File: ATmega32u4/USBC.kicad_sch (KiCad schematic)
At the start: 6 parts, among them J1 USB_C_Receptacle_USB2.0, U4 USBLC6-2SC6

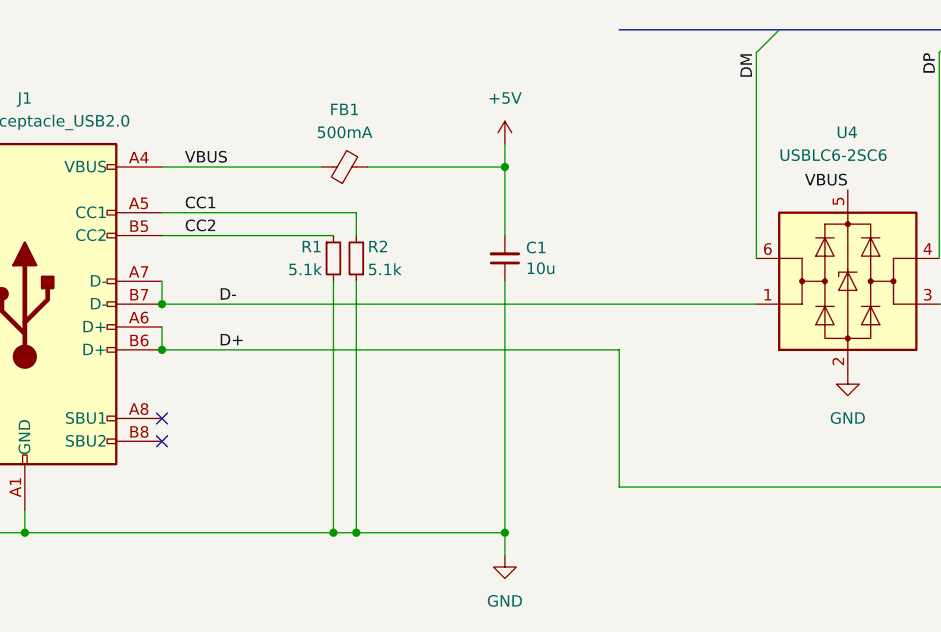
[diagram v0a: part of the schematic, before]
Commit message: Review and updates to power path
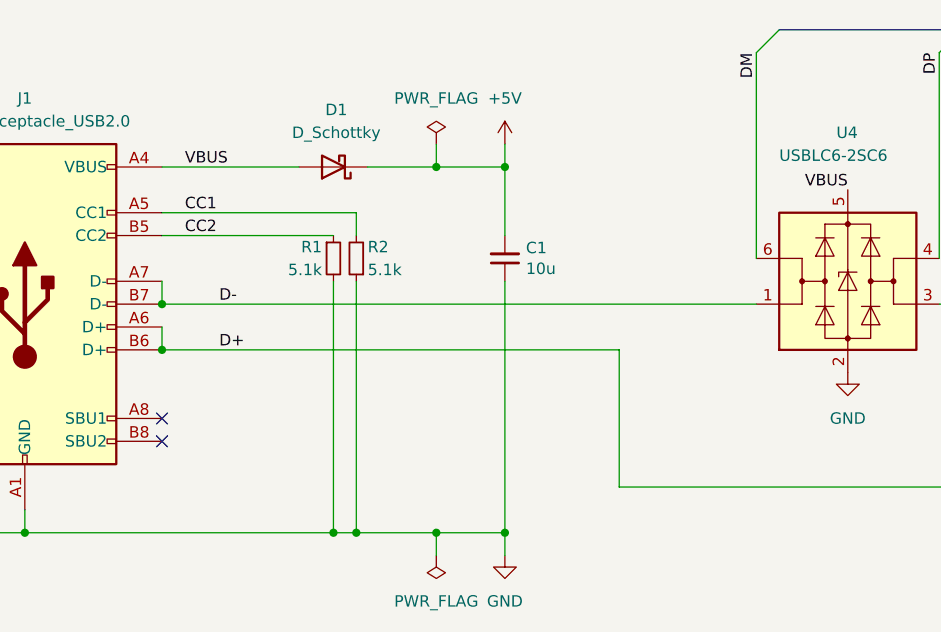
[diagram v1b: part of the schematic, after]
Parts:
- removed FB1: 500mA, Inductor_SMD:L_0805_2012Metric, symbol Device:FerriteBead_Small
- added D1: D_Schottky, Diode_SMD:D_SOD-323, symbol Device:D_Schottky
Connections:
- net +5V: now also D1.1 (K)
- net VBUS: now also D1.2 (A)
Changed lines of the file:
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@@
   (junction (at 165.1 106.68) (diameter 0) (color 0 0 0 0)
+  )
+  (junction (at 157.48 106.68) (diameter 0) (color 0 0 0 0)
+  )
+  (junction (at 157.48 66.04) (diameter 0) (color 0 0 0 0)
   )
   (junction (at 111.76 106.68) (diameter 0) (color 0 0 0 0)
@@
     (stroke (width 0) (type default) (color 0 0 0 0))
   )
-  (wire (pts (xy 148.59 106.68) (xy 165.1 106.68))
+  (wire (pts (xy 157.48 106.68) (xy 165.1 106.68))
     (stroke (width 0) (type default) (color 0 0 0 0))
   )
@@
     (stroke (width 0) (type default) (color 0 0 0 0))
   )
+  (wire (pts (xy 157.48 109.22) (xy 157.48 106.68))
+    (stroke (width 0) (type default) (color 0 0 0 0))
+  )
   (wire (pts (xy 104.14 106.68) (xy 111.76 106.68))
     (stroke (width 0) (type default) (color 0 0 0 0))
@@
     (stroke (width 0) (type default) (color 0 0 0 0))
   )
-  (bus (pts (xy 177.8 50.8) (xy 195.58 50.8))
-    (stroke (width 0) (type default) (color 0 0 0 0))
-  )
   (wire (pts (xy 148.59 78.74) (xy 148.59 106.68))
     (stroke (width 0) (type default) (color 0 0 0 0))
@@
     (stroke (width 0) (type default) (color 0 0 0 0))
   )
+  (wire (pts (xy 148.59 106.68) (xy 157.48 106.68))
+    (stroke (width 0) (type default) (color 0 0 0 0))
+  )
   (wire (pts (xy 165.1 109.22) (xy 165.1 106.68))
     (stroke (width 0) (type default) (color 0 0 0 0))
   )
-  (wire (pts (xy 127 66.04) (xy 144.78 66.04))
+  (wire (pts (xy 127 66.04) (xy 142.24 66.04))
+    (stroke (width 0) (type default) (color 0 0 0 0))
+  )
+  (wire (pts (xy 157.48 66.04) (xy 165.1 66.04))
     (stroke (width 0) (type default) (color 0 0 0 0))
   )
@@
     (stroke (width 0) (type default) (color 0 0 0 0))
   )
-  (wire (pts (xy 149.86 66.04) (xy 165.1 66.04))
+  (wire (pts (xy 157.48 63.5) (xy 157.48 66.04))
+    (stroke (width 0) (type default) (color 0 0 0 0))
+  )
+  (wire (pts (xy 149.86 66.04) (xy 157.48 66.04))
     (stroke (width 0) (type default) (color 0 0 0 0))
   )
@@
     )
     (property "Datasheet" "" (id 3) (at 203.2 88.9 0)
+      (effects (font (size 1.27 1.27)) hide)
+    )
+    (pin "1")
+  )
+  (symbol (lib_id "power:PWR_FLAG") (at 157.48 63.5 0) (unit 1)
+    (in_bom yes) (on_board yes) (fields_autoplaced)
+    (property "Reference" "#FLG01" (id 0) (at 157.48 61.595 0)
+      (effects (font (size 1.27 1.27)) hide)
+    )
+    (property "Value" "PWR_FLAG" (id 1) (at 157.48 58.42 0))
+    (property "Footprint" "" (id 2) (at 157.48 63.5 0)
+      (effects (font (size 1.27 1.27)) hide)
+    )
+    (property "Datasheet" "~" (id 3) (at 157.48 63.5 0)
       (effects (font (size 1.27 1.27)) hide)
     )
@@
     )
     (property "Datasheet" "~" (id 3) (at 148.59 76.2 0)
-      (effects (font (size 1.27 1.27)) hide)
-    )
-    (pin "1")
-    (pin "2")
-  )
-  (symbol (lib_id "Device:FerriteBead_Small") (at 147.32 66.04 90) (unit 1)
-    (in_bom yes) (on_board yes) (fields_autoplaced)
-    (property "Reference" "FB1" (id 0) (at 147.2819 59.69 90))
-    (property "Value" "500mA" (id 1) (at 147.2819 62.23 90))
-    (property "Footprint" "Inductor_SMD:L_0805_2012Metric" (id 2) (at 147.32 67.818 90)
-      (effects (font (size 1.27 1.27)) hide)
-    )
-    (property "Datasheet" "~" (id 3) (at 147.32 66.04 0)
       (effects (font (size 1.27 1.27)) hide)
     )
@@
     (pin "6")
   )
+  (symbol (lib_id "Device:D_Schottky") (at 146.05 66.04 180) (unit 1)
+    (in_bom yes) (on_board yes) (fields_autoplaced)
+    (property "Reference" "D1" (id 0) (at 146.3675 59.69 0))
+    (property "Value" "D_Schottky" (id 1) (at 146.3675 62.23 0))
+    (property "Footprint" "Diode_SMD:D_SOD-323" (id 2) (at 146.05 66.04 0)
+      (effects (font (size 1.27 1.27)) hide)
+    )
+    (property "Datasheet" "~" (id 3) (at 146.05 66.04 0)
+      (effects (font (size 1.27 1.27)) hide)
+    )
+    (pin "1")
+    (pin "2")
+  )
+  (symbol (lib_id "power:PWR_FLAG") (at 157.48 109.22 180) (unit 1)
+    (in_bom yes) (on_board yes) (fields_autoplaced)
+    (property "Reference" "#FLG03" (id 0) (at 157.48 111.125 0)
+      (effects (font (size 1.27 1.27)) hide)
+    )
+    (property "Value" "PWR_FLAG" (id 1) (at 157.48 114.3 0))
+    (property "Footprint" "" (id 2) (at 157.48 109.22 0)
+      (effects (font (size 1.27 1.27)) hide)
+    )
+    (property "Datasheet" "~" (id 3) (at 157.48 109.22 0)
+      (effects (font (size 1.27 1.27)) hide)
+    )
+    (pin "1")
+  )
   (symbol (lib_id "Device:C_Small") (at 165.1 76.2 180) (unit 1)

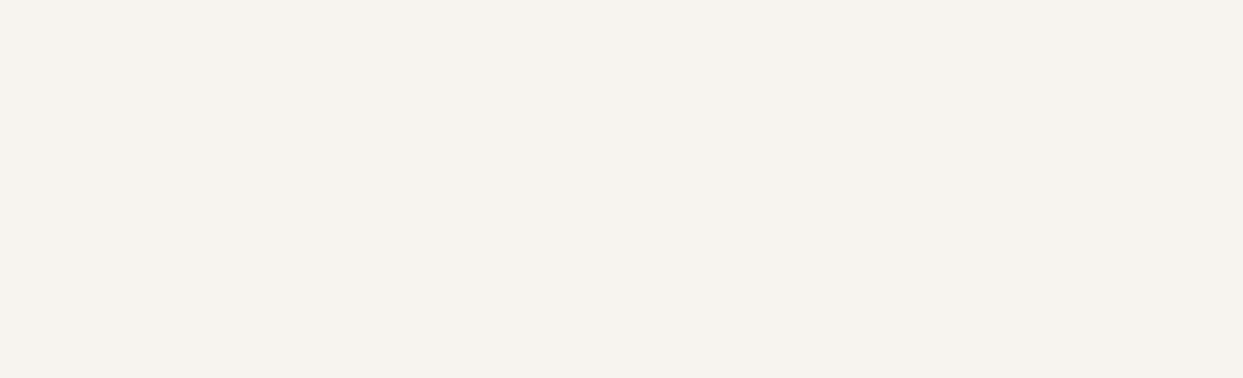
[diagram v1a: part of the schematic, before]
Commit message: Schematic, routing and layout changes post review.
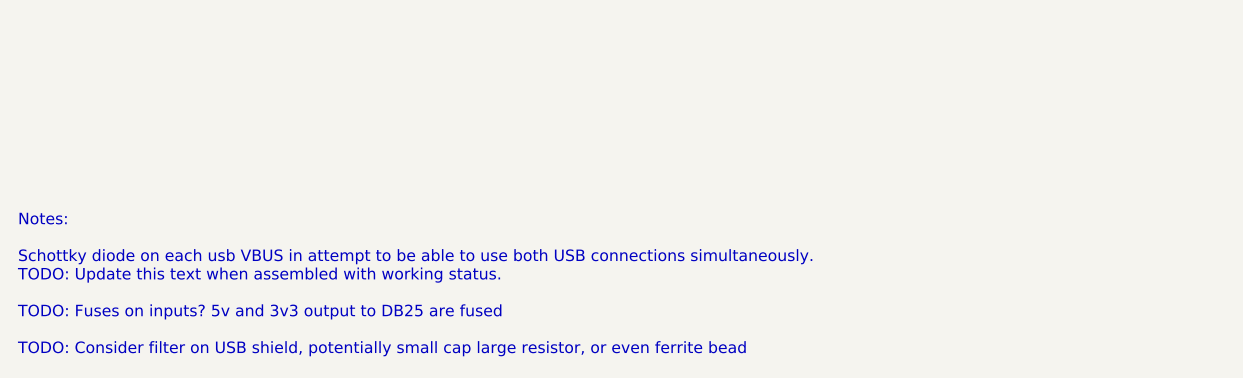
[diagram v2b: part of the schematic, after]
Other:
- note added: "Notes: Schottky diode on each usb VBUS in attempt to be able to use both USB connections simultaneously. TODO: Update this text when assembled with working status. TODO: Fuses on inputs? 5v and 3v3 output to DB25 are fused TODO: Consider filter on USB shield, potentially small cap large resistor, or even ferrite bead"
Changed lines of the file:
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@@
     (stroke (width 0) (type default) (color 0 0 0 0))
+  )
+  (text "Notes:\n\nSchottky diode on each usb VBUS in attempt to be able to use both USB connections simultaneously.\nTODO: Update this text when assembled with working status.\n\nTODO: Fuses on inputs? 5v and 3v3 output to DB25 are fused\n\nTODO: Consider filter on USB shield, potentially small cap large resistor, or even ferrite bead"
+    (at 13.97 195.58 0)
+    (effects (font (size 1.27 1.27)) (justify left bottom))
   )
   (label "D+" (at 133.35 86.36 0)

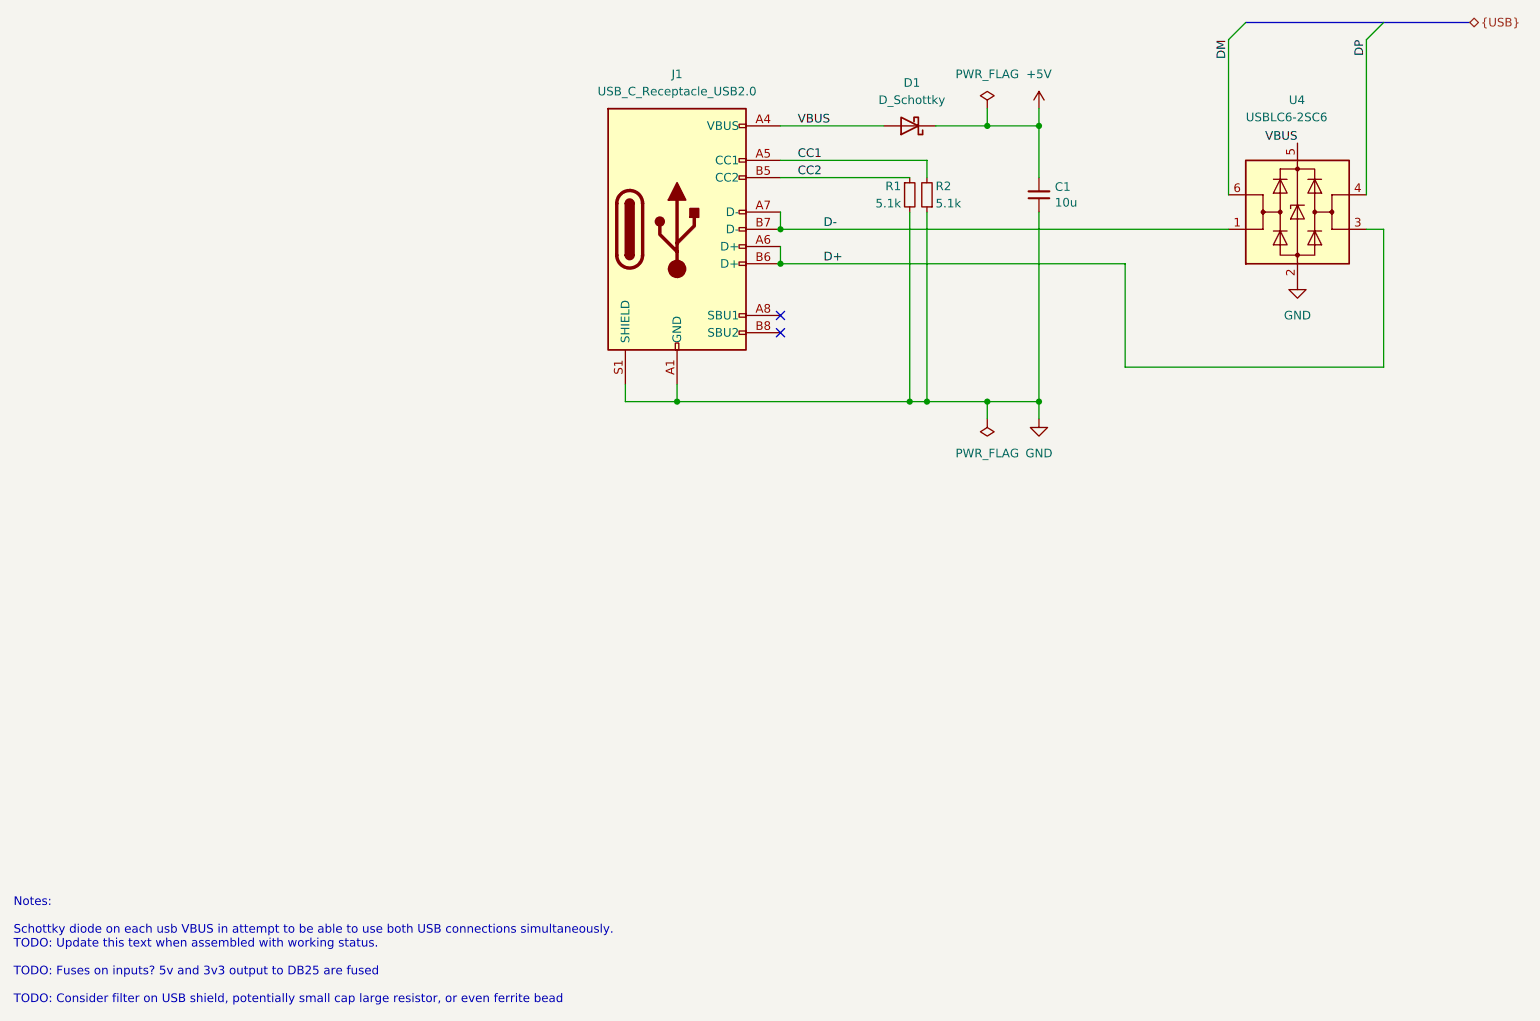
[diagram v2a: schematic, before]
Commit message: Update notes, add io for reading cc pins, minor changes to schematic and routing.
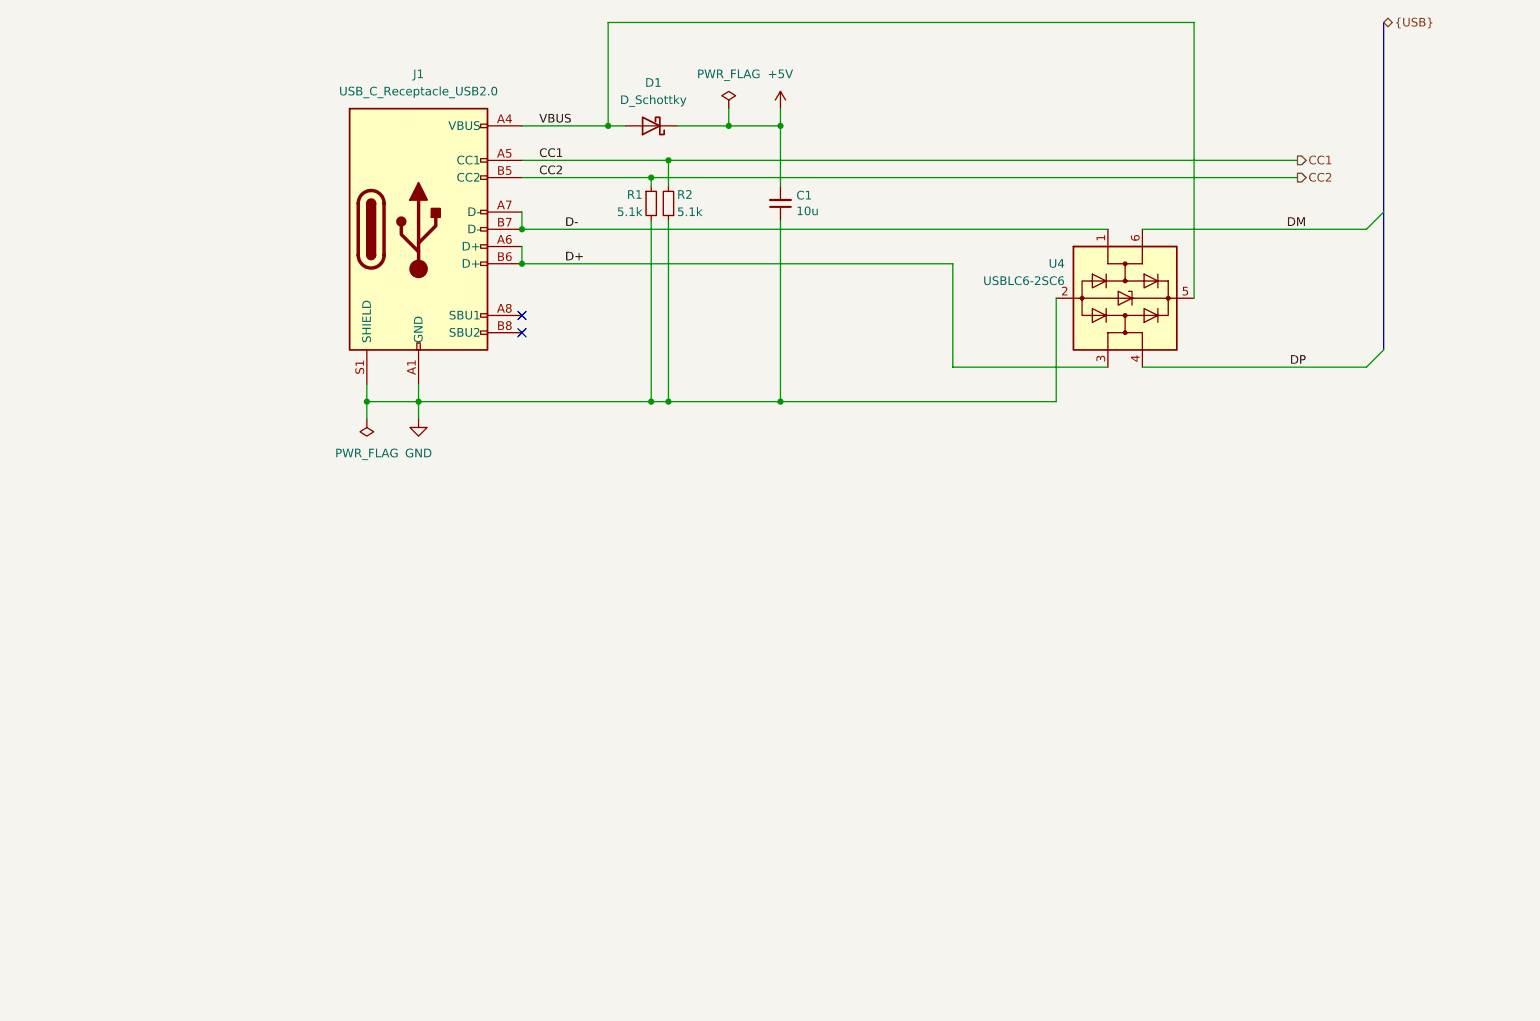
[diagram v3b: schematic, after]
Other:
- note removed: "Notes: Schottky diode on each usb VBUS in attempt to be able to use both USB connections simultaneously. TODO: Update this text when assembled with working status. TODO: Fuses on inputs? 5v and 3v3 output to DB25 are fused TODO: Consider filter on USB shield, potentially small cap large resistor, or even ferrite bead"
- title: (none) -> OpenRetroPad
- moved on the sheet: C1, D1, J1, R1, R2, U4
